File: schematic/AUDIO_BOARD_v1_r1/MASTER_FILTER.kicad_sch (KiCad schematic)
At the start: 66 parts, among them U30 OPA1678, U31 LM13700, U32 LM13700, U33 4052, U34 OPA1678, U35 LM13700, U36 LM13700, U37 4052

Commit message: render!
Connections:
- net BPL: now also R113.1
- net BPR: now also R213.1
- net LPL: now also R117.1
- net LPR: now also R217.1
- net at R201.2: now also R200.2, R202.2, R203.1, U34.2 (-)
- net at R100.2, R102.2, R103.1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: now also R101.2
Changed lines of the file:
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@@
 		)
 	)
+	(wire
+		(pts
+			(xy 29.21 64.77) (xy 29.21 72.39)
+		)
+		(stroke
+			(width 0)
+			(type default)
+		)
+	)
+	(wire
+		(pts
+			(xy 29.21 194.31) (xy 29.21 201.93)
+		)
+		(stroke
+			(width 0)
+			(type default)
+		)
+	)
+	(junction
+		(at 148.59 60.96)
+		(diameter 0)
+		(color 0 0 0 0)
+	)
+	(junction
+		(at 148.59 88.9)
+		(diameter 0)
+		(color 0 0 0 0)
+	)
+	(junction
+		(at 148.59 190.5)
+		(diameter 0)
+		(color 0 0 0 0)
+	)
+	(junction
+		(at 148.59 218.44)
+		(diameter 0)
+		(color 0 0 0 0)
+	)
 )

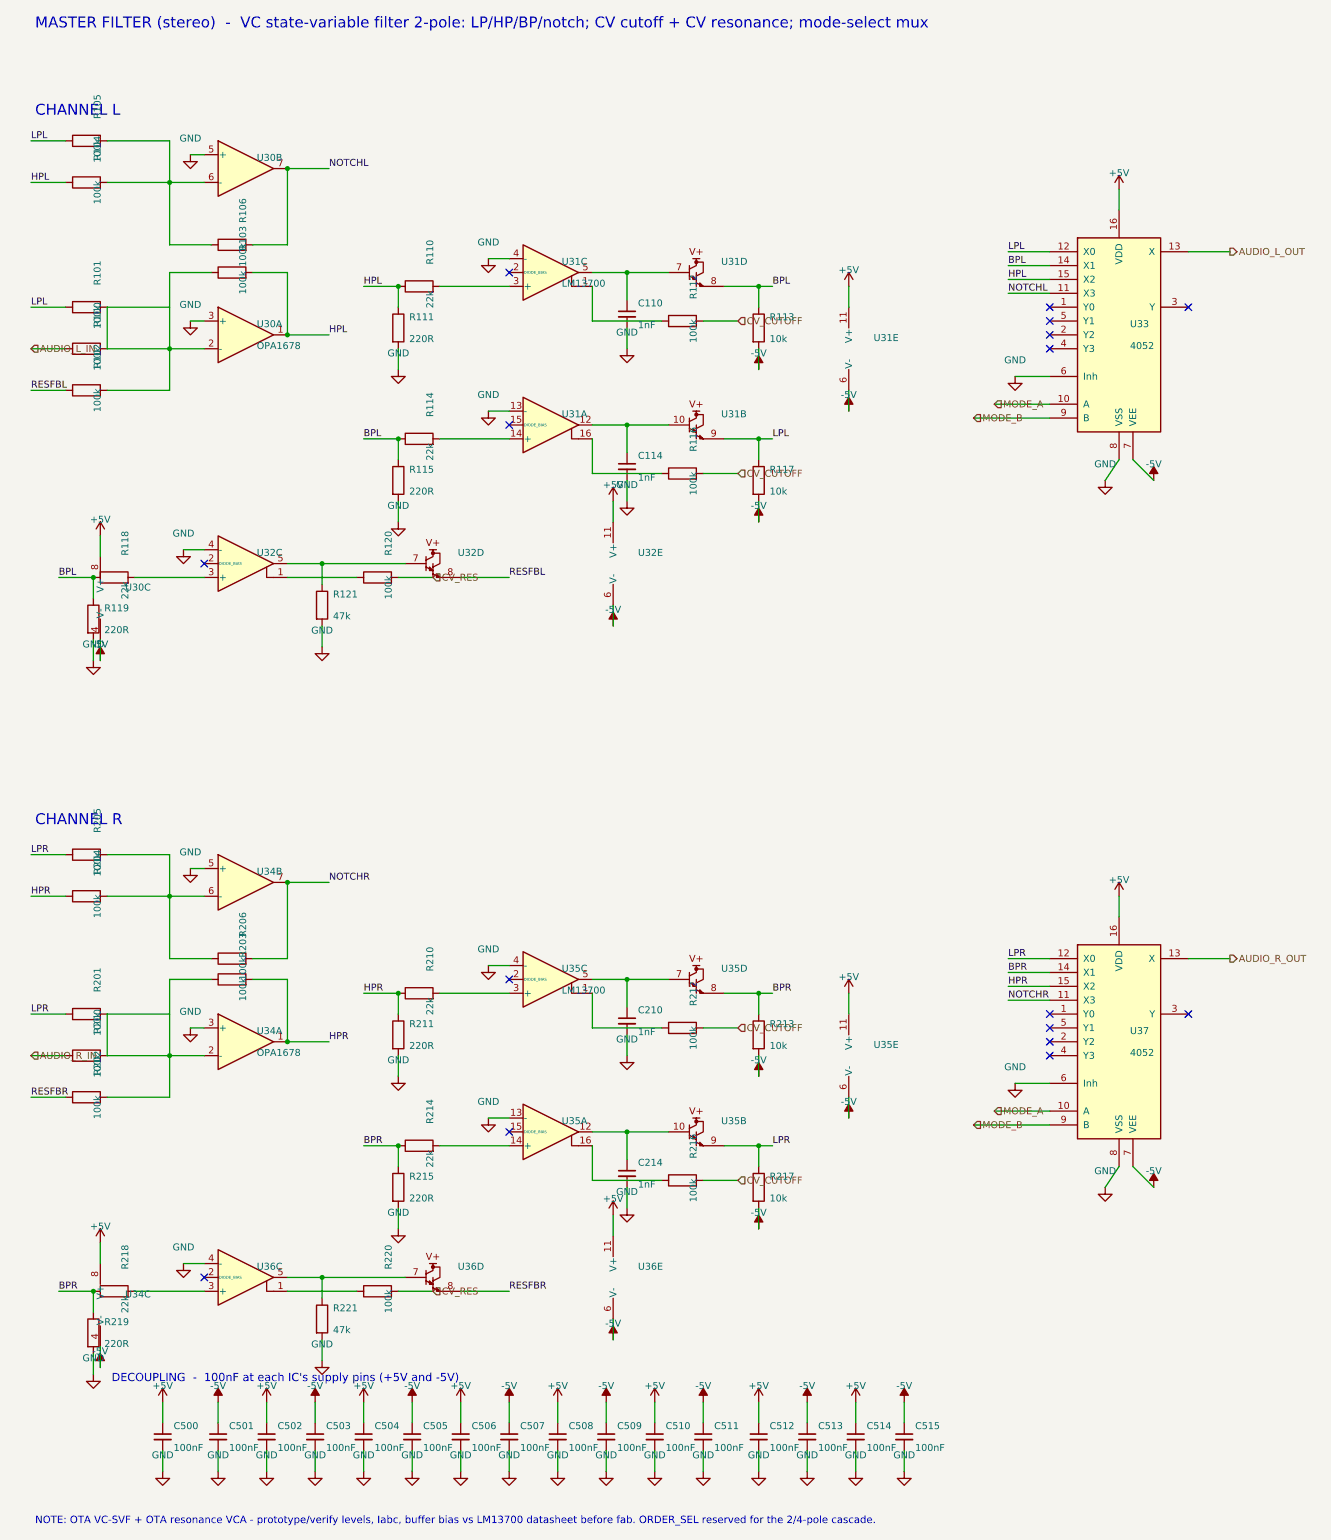
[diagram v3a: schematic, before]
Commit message: more placement and routing
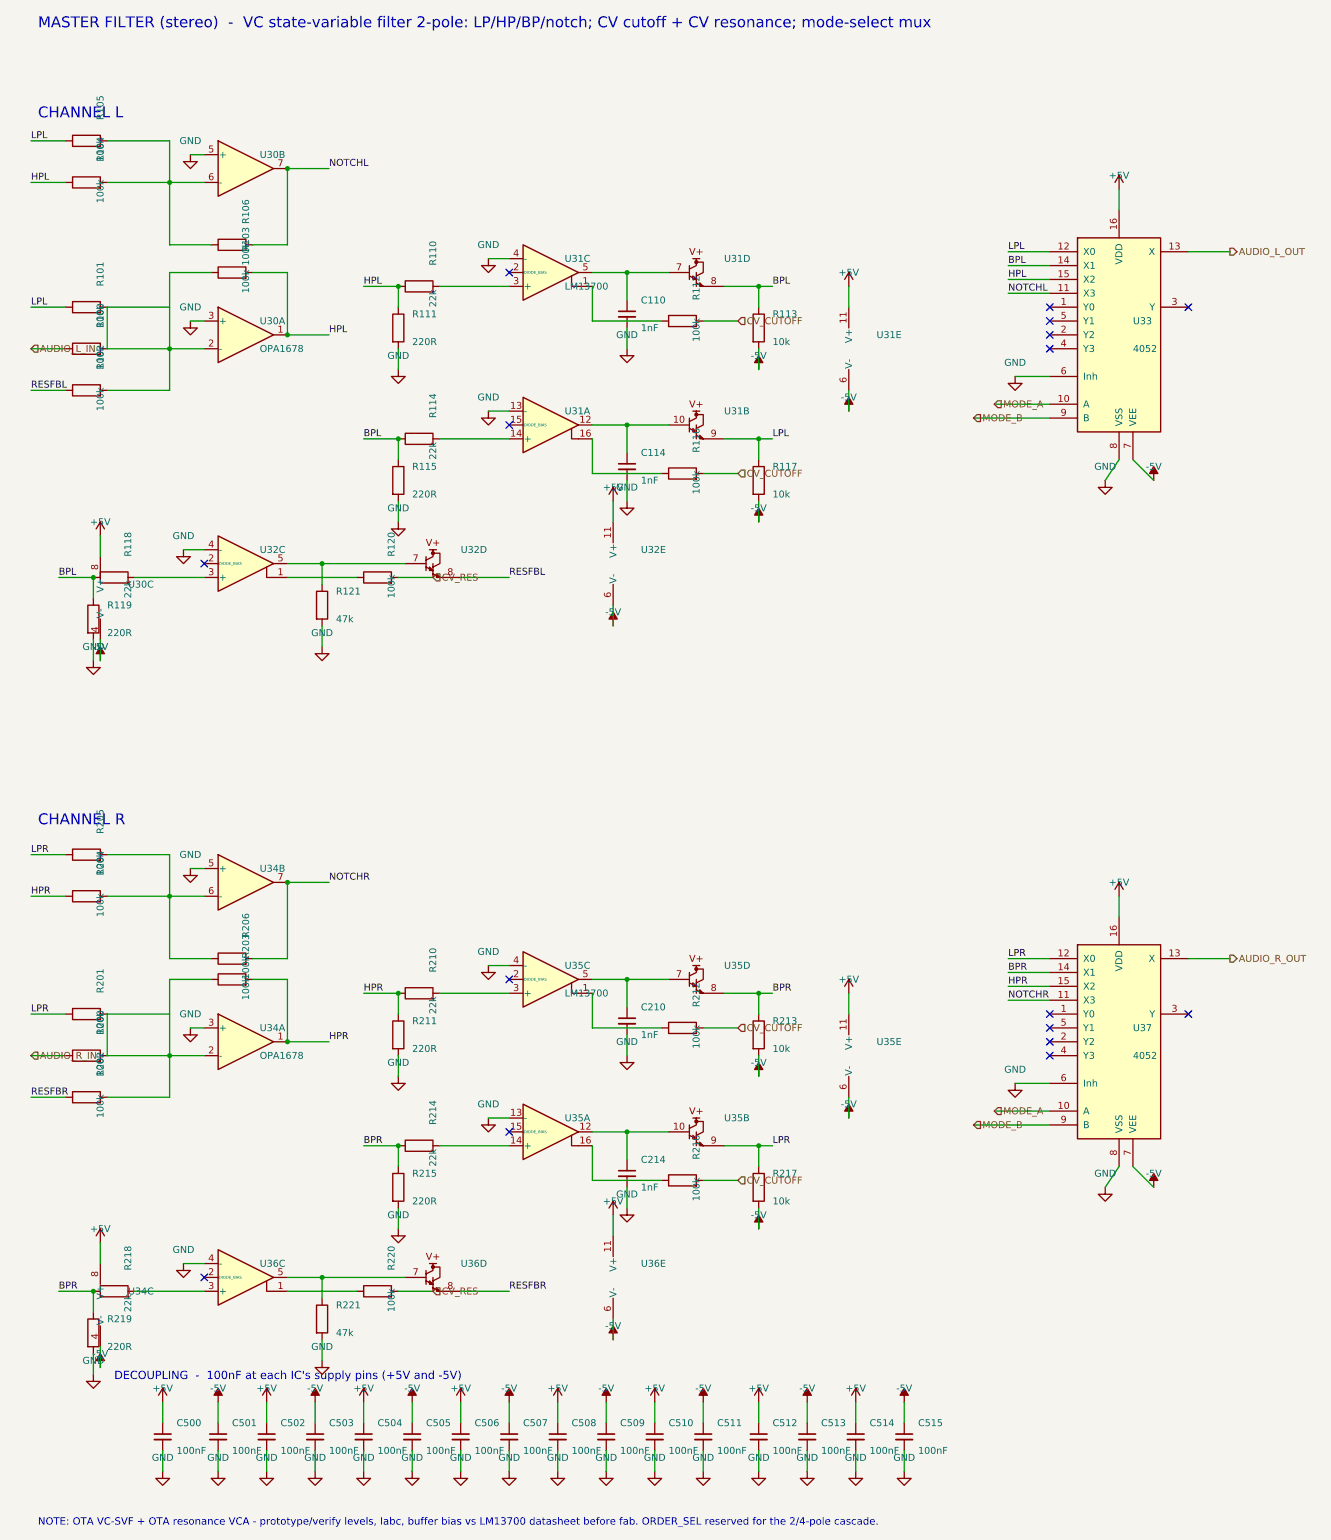
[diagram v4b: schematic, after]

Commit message: placement. start with each sheet for the most part
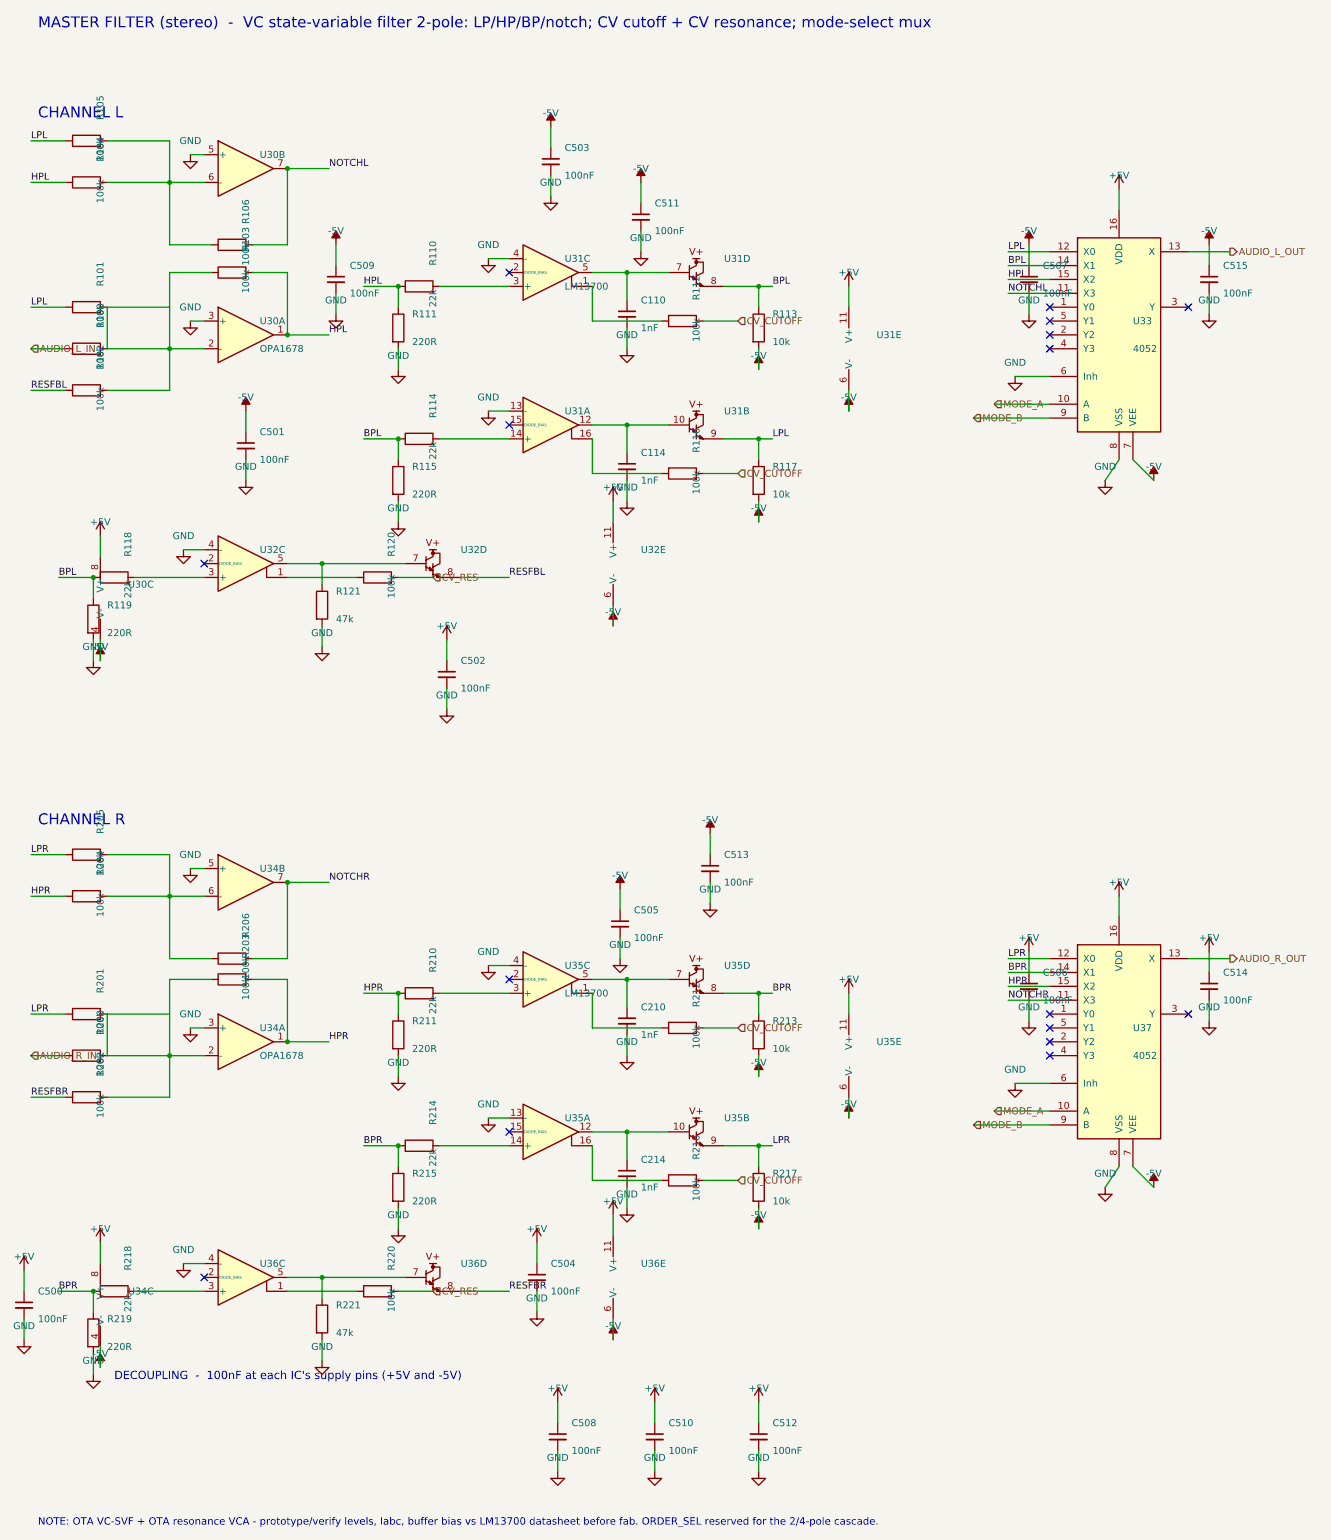
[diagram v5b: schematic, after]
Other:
- moved on the sheet: C500, C501, C502, C503, C504, C505, C506, C507, C509, C511, C513, C514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

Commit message: try autorouter?
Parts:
- U30, U34: footprint Package_DIP:DIP-8_W7.62mm_SMDSocket_SmallPads -> Package_SO:SOIC-8_3.9x4.9mm_P1.27mm
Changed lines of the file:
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@@
 			)
 		)
-		(property "Footprint" "Package_DIP:DIP-8_W7.62mm_SMDSocket_SmallPads"
+		(property "Footprint" "Package_SO:SOIC-8_3.9x4.9mm_P1.27mm"
 			(at 54.61 69.85 0)
 			(hide yes)
@@
 			)
 		)
-		(property "Footprint" "Package_DIP:DIP-8_W7.62mm_SMDSocket_SmallPads"
+		(property "Footprint" "Package_SO:SOIC-8_3.9x4.9mm_P1.27mm"
 			(at 54.61 199.39 0)
 			(hide yes)
